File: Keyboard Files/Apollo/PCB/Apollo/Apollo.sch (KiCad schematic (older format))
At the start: 198 parts, among them J1 AVR-ISP-6, J10 Conn_01x01, J11 Conn_01x01, J12 Conn_01x01, J13 Conn_01x01, J14 Conn_01x01, J15 Conn_01x01, J16 Conn_01x01, J2 AVR-ISP-6, J3 Conn_01x01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

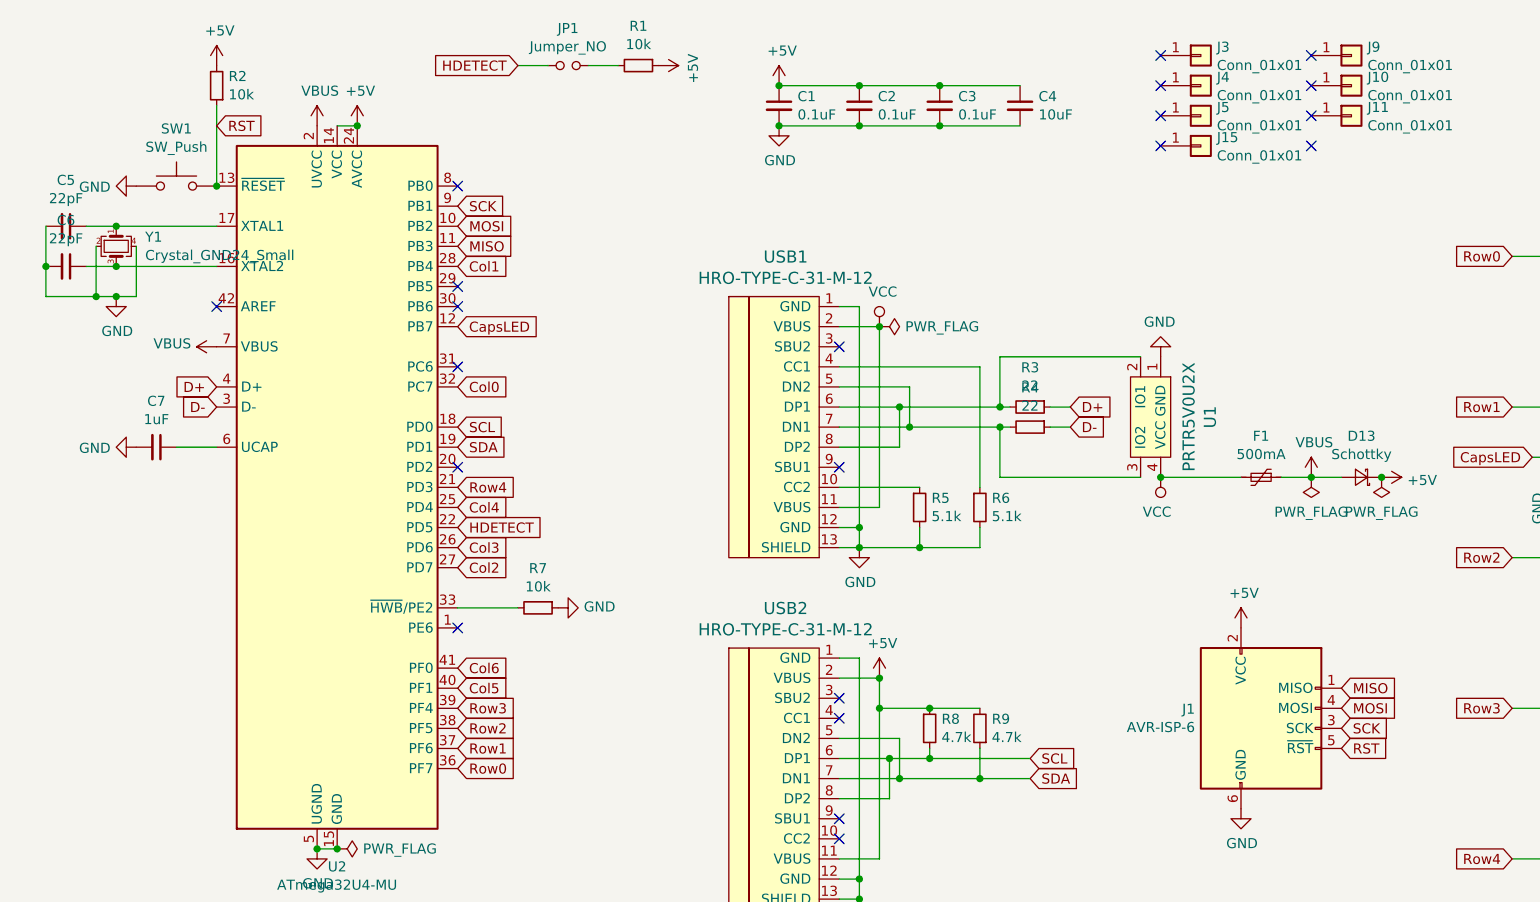
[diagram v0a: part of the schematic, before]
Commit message: Increase Apollo plate bezel
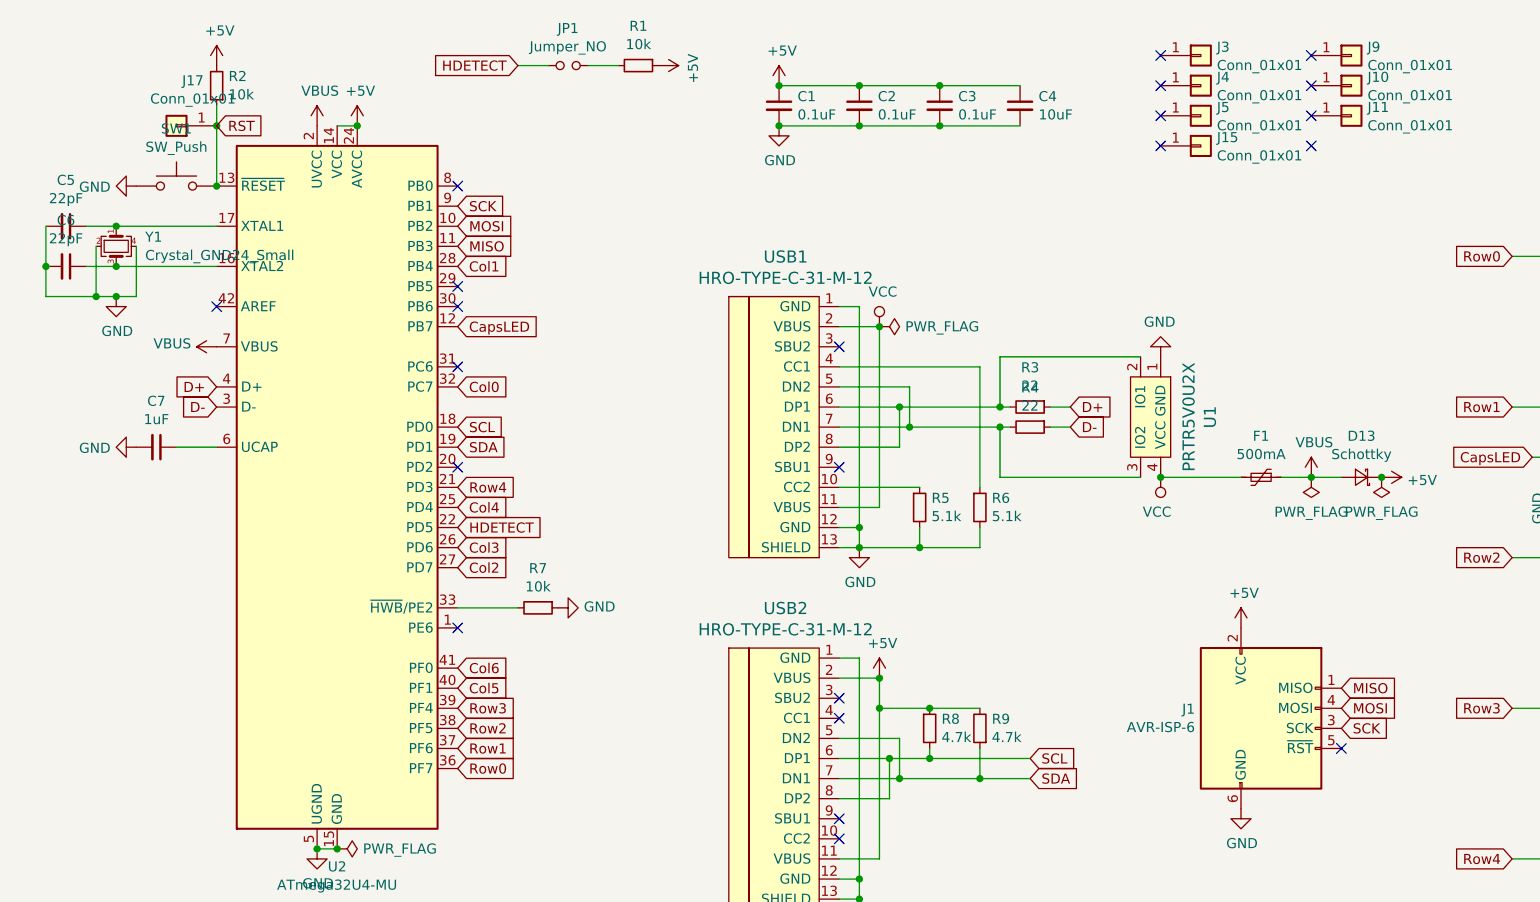
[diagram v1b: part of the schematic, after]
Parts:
- added J17: Conn_01x01, Connector_PinHeader_2.54mm:PinHeader_1x01_P2.54mm_Vertical, symbol Connector_Generic:Conn_01x01
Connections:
- net RST: now also J17.1 (Pin_1); no longer J1.5 (~RST)
- no-connect marks 43 -> 44
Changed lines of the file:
@@
 $EndComp
 Wire Wire Line
-	1500 1050 1500 1450
+	1500 1050 1500 1150
 Connection ~ 1500 1450
 Wire Wire Line
@@
 Text GLabel 7100 4150 2    50   Input ~ 0
 SCK
-Text GLabel 7100 4250 2    50   Input ~ 0
-RST
 $Comp
 L Type-C:HRO-TYPE-C-31-M-12 USB1
@@
 NoConn ~ 7000 6500
 NoConn ~ 2750 8250
+$Comp
+L Connector_Generic:Conn_01x01 J17
+U 1 1 5E579A3D
+P 1300 1150
+F 0 "J17" H 1218 925 50  0000 C CNN
+F 1 "Conn_01x01" H 1218 1016 50  0000 C CNN
+F 2 "Connector_PinHeader_2.54mm:PinHeader_1x01_P2.54mm_Vertical" H 1300 1150 50  0001 C CNN
+F 3 "~" H 1300 1150 50  0001 C CNN
+	1    1300 1150
+	-1   0    0    1
+$EndComp
+Connection ~ 1500 1150
+Wire Wire Line
+	1500 1150 1500 1450
+NoConn ~ 7100 4250
 $EndSCHEMATC
